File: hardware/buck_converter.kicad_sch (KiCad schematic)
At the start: 0 parts

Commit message: Adjust values of the components
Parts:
- added C1, C2, C5, C6, C7, C8, C9: 100nF, symbol Device:C
- added C3: 10µF, symbol Device:C_Polarized
- added C4: 47µF, symbol Device:C_Polarized
- added D1: 1N4007, symbol Diode:1N4007
- added D2: LED, symbol Device:LED
- added DS1: WC1602, symbol Display_Character:WC1602A
- added J1: In, symbol Connector_Generic:Conn_01x02
- added J2: Out, symbol Connector_Generic:Conn_01x02
- added J3: Nucleo, symbol Connector_Generic:Conn_02x14_Odd_Even
- added J4: MicroSD Card, symbol Connector:Micro_SD_Card
- added L1: 100µH, symbol Device:L
- added LDR1: Photo, symbol Device:R_Photo
- added Q1: IRF9540N, symbol Transistor_FET:IRF9540N
- added Q2: BC547, symbol Transistor_BJT:BC547
- added R1: 0.1Ω (5W), symbol Device:R
- added R10, R7: 100Ω, symbol Device:R
- added R11, R2, R3, R6, R8, R9: 1kΩ, symbol Device:R
- added R12: 300Ω, symbol Device:R
- added R13, R4: 10kΩ, symbol Device:R
- added R5: 8.2kΩ, symbol Device:R
- added RV1: 10kΩ, symbol Device:R_Potentiometer_Trim
- added SW1: Preset #1, symbol Switch:SW_Push
- added SW2: Preset #2, symbol Switch:SW_Push
- added SW3: Encoder, symbol Device:RotaryEncoder_Switch
- added SW4: Preset #3, symbol Switch:SW_Push
- added SW5: Preset #4, symbol Switch:SW_Push
- added U1, U2: LM358, symbol Amplifier_Operational:LM358
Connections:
- new net: D1.1 (K), L1.1, Q1.2 (D)
- new net: C4.1, C5.1, J2.1 (Pin_1), L1.2, R5.1
- new net: Q2.2 (B), R11.1
- new net: C3.1, J1.1 (Pin_1), Q1.3 (S), R4.1
- new net: Q1.1 (G), R4.2, R7.2
- new net: DS1.16 (LED(-)), R10.1
- new net: Q2.1 (C), R10.2
- new net: R8.1, U2.1, U2.2 (-)
- new net: C7.1, R8.2, R9.1
- new net: C9.1, R9.2, U2.5 (+)
- new net: C1.1, R2.2, R3.1
- new net: C6.1, R3.2, U1.5 (+)
- new net: DS1.3 (VO), RV1.2
- new net: R2.1, U1.1, U1.2 (-)
- new net: D2.2 (A), R12.2
- new net +3.3V: C2.1, C8.1, DS1.15 (LED(+)), DS1.2 (VDD), J3.2 (Pin_2), J4.4 (VDD), LDR1.1, RV1.1, U1.8 (V+), U2.8 (V+)
- new net BCKL: J3.3 (Pin_3), R11.2
- new net CURRENT: C7.2, J3.9 (Pin_9), U2.6 (-), U2.7
- new net GND: C2.2, C3.2, C4.2, C5.2, C6.2, C8.2, C9.2, D1.2 (A), D2.1 (K), DS1.1 (VSS), DS1.5 (R/W), J1.2 (Pin_2), J3.28 (Pin_28), J4.6 (VSS), J4.9 (SHIELD), Q2.3 (E), R1.1, R13.2, R6.2, RV1.3, SW1.2, SW2.2, SW3.C, SW3.S2, SW4.2, SW5.2, U1.4 (V-), U2.4 (V-)
- new net INT1: J3.19 (Pin_19), SW3.A
- new net INT2: J3.21 (Pin_21), SW3.B
- new net I_{out}: J2.2 (Pin_2), R1.2, U2.3 (+)
- new net KEY: J3.1 (Pin_1), R7.1
- new net LCD_D4: DS1.11 (D4), J3.8 (Pin_8)
- new net LCD_D5: DS1.12 (D5), J3.10 (Pin_10)
- new net LCD_D6: DS1.13 (D6), J3.12 (Pin_12)
- new net LCD_D7: DS1.14 (D7), J3.14 (Pin_14)
- new net LCD_E: DS1.6 (E), J3.4 (Pin_4)
- new net LCD_RS: DS1.4 (RS), J3.6 (Pin_6)
- new net OC_LED: J3.25 (Pin_25), R12.1
- new net PHOTO: J3.5 (Pin_5), LDR1.2, R13.1
- new net SDMMC_CLK: J3.18 (Pin_18), J4.5 (CLK)
- new net SDMMC_CMD: J3.16 (Pin_16), J4.3 (CMD)
- new net SDMMC_D0: J3.20 (Pin_20), J4.7 (DAT0)
- new net SDMMC_D1: J3.22 (Pin_22), J4.8 (DAT1)
- new net SDMMC_D2: J3.24 (Pin_24), J4.1 (DAT2)
- new net SDMMC_D3: J3.26 (Pin_26), J4.2 (DAT3/CD)
- new net SW1: J3.11 (Pin_11), SW1.1
- new net SW2: J3.13 (Pin_13), SW2.1
- new net SW3: J3.15 (Pin_15), SW4.1
- new net SW4: J3.17 (Pin_17), SW5.1
- new net SW5: J3.23 (Pin_23), SW3.S1
- new net VOLTAGE: C1.2, J3.7 (Pin_7), U1.6 (-), U1.7
- new net V_{out}: R5.2, R6.1, U1.3 (+)
- no-connect marks 0 -> 5
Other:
- note added: "Converter"
- note added: "For ERC"
- note added: "Input"
- note added: "LCD"
- note added: "Light sensor"
- note added: "Low-pass filters"
- note added: "Max. 3.261V"
- note added: "Nucleo Board"
- note added: "OC LED"
- note added: "SD Card"
- note added: "f_{c} ≈ 1.5kHz"

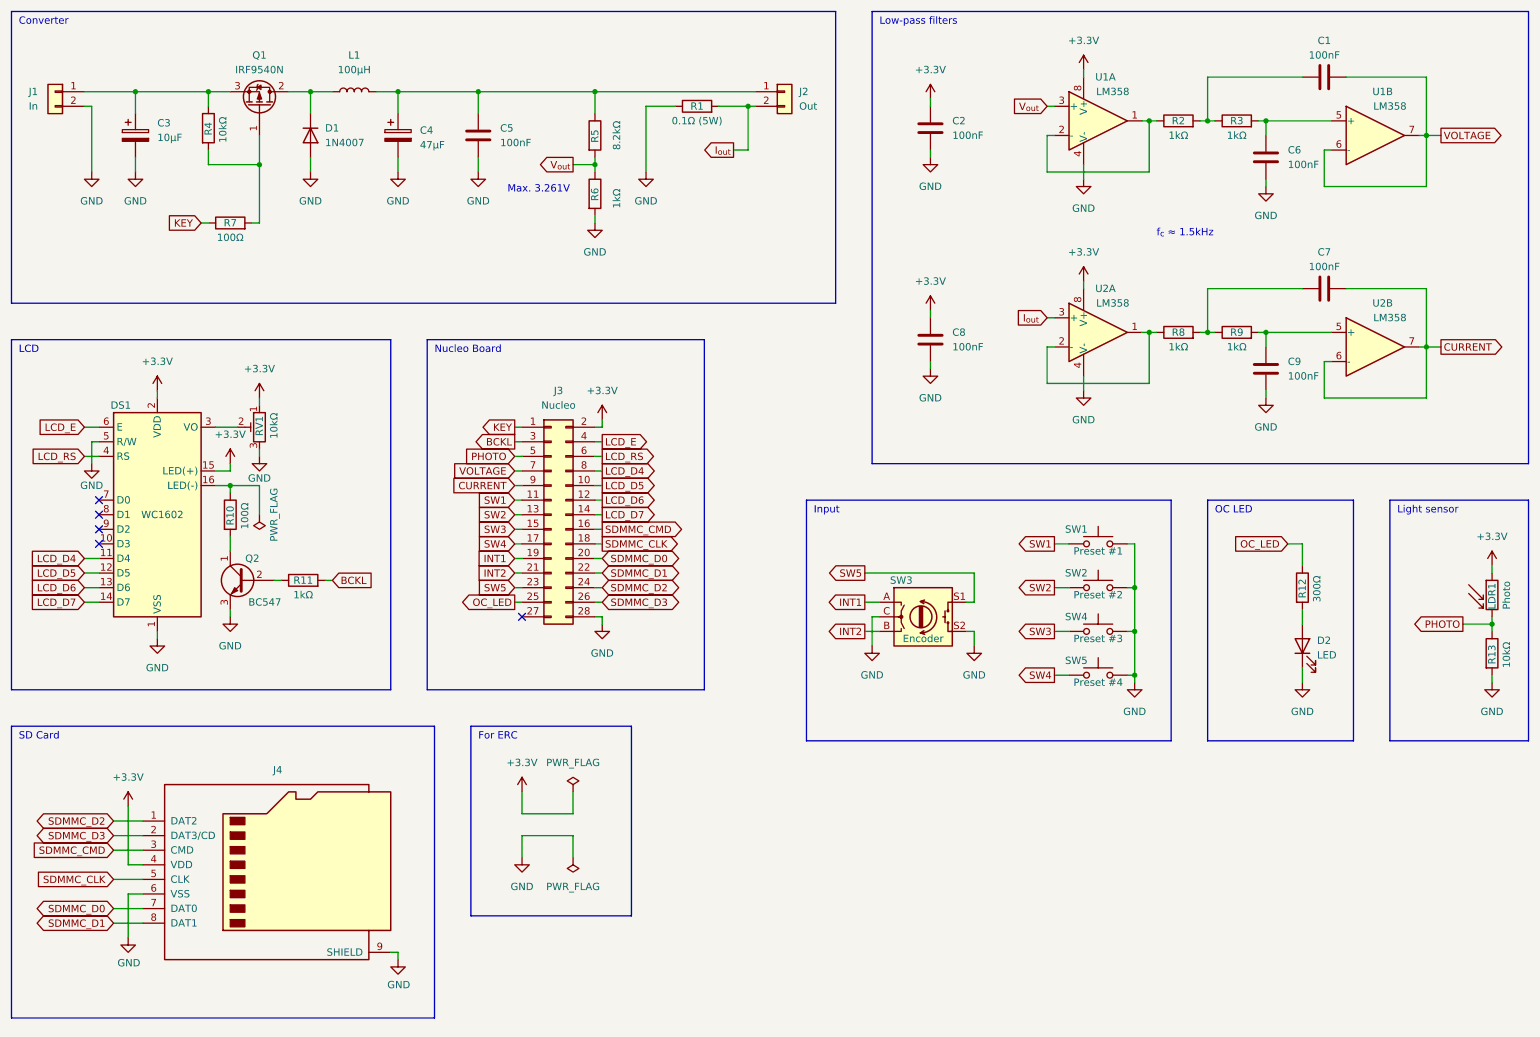
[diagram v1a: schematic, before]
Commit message: Add buttons and LEDs to the configuration
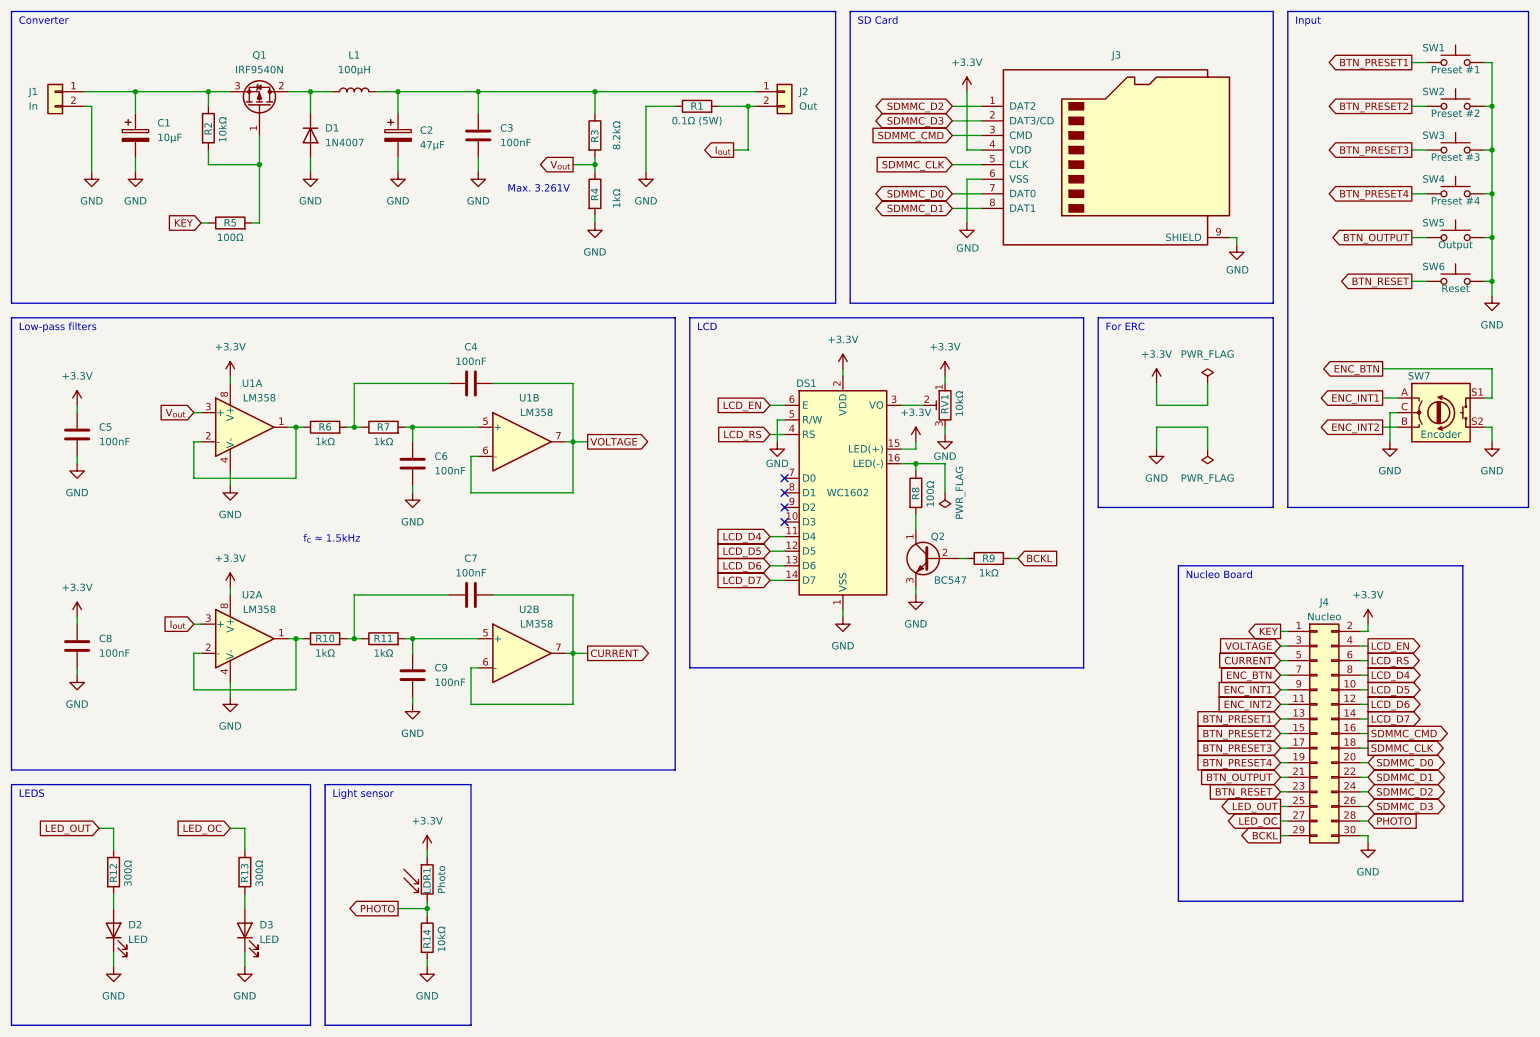
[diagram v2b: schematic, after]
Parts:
- added D3: LED, symbol Device:LED
- added R13: 300Ω, symbol Device:R
- added SW5: Output, symbol Switch:SW_Push
- added SW6: Reset, symbol Switch:SW_Push
- J4: renamed from J3; symbol Connector_Generic:Conn_02x14_Odd_Even -> Connector_Generic:Conn_02x15_Odd_Even
- renumbered C3 to C1, C4 to C2, C5 to C3, C1 to C4, C2 to C5, J4 to J3, R8 to R10, R9 to R11, R13 to R14, R4 to R2, R5 to R3, R6 to R4, R7 to R5, R2 to R6, R3 to R7, R10 to R8, R11 to R9, SW4 to SW3, SW5 to SW4, SW3 to SW7
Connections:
- net BCKL: now also J4.29 (Pin_29); no longer J4.3 (Pin_3)
- net CURRENT: now also J4.5 (Pin_5); no longer J4.9 (Pin_9)
- net GND: now also J4.30 (Pin_30), D3.1 (K), SW5.2, SW6.2; no longer J4.28 (Pin_28)
- net PHOTO: now also J4.28 (Pin_28); no longer J4.5 (Pin_5)
- net VOLTAGE: now also J4.3 (Pin_3); no longer J4.7 (Pin_7)
- net LED_OC: now reaches J4.27 (Pin_27)
- net LED_OC: now also R13.1
- net INT1 renamed BTN_PRESET4
- net BTN_PRESET4: now also SW4.1; no longer SW7.A
- net INT2 renamed BTN_OUTPUT
- net BTN_OUTPUT: now also SW5.1; no longer SW7.B
- net LCD_E renamed LCD_EN
- net OC_LED renamed LED_OUT
- net SW1 renamed BTN_PRESET1
- net BTN_PRESET1: now also J4.13 (Pin_13); no longer J4.11 (Pin_11)
- net SW2 renamed BTN_PRESET2
- net BTN_PRESET2: now also J4.15 (Pin_15); no longer J4.13 (Pin_13)
- net SW3 renamed BTN_PRESET3
- net BTN_PRESET3: now also J4.17 (Pin_17); no longer J4.15 (Pin_15)
- removed net SW4: J4.17 (Pin_17), SW4.1
- net SW5 renamed BTN_RESET
- net BTN_RESET: now also SW6.1; no longer SW7.S1
- new net: D3.2 (A), R13.2
- new net ENC_BTN: J4.7 (Pin_7), SW7.S1
- new net ENC_INT1: J4.9 (Pin_9), SW7.A
- new net ENC_INT2: J4.11 (Pin_11), SW7.B
- no-connect marks 5 -> 4
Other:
- note added: "LEDS"
- note removed: "OC LED"
- moved on the sheet: C4, C5, C6, C7, C8, C9, D2, DS1, J3, LDR1, Q2, R10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

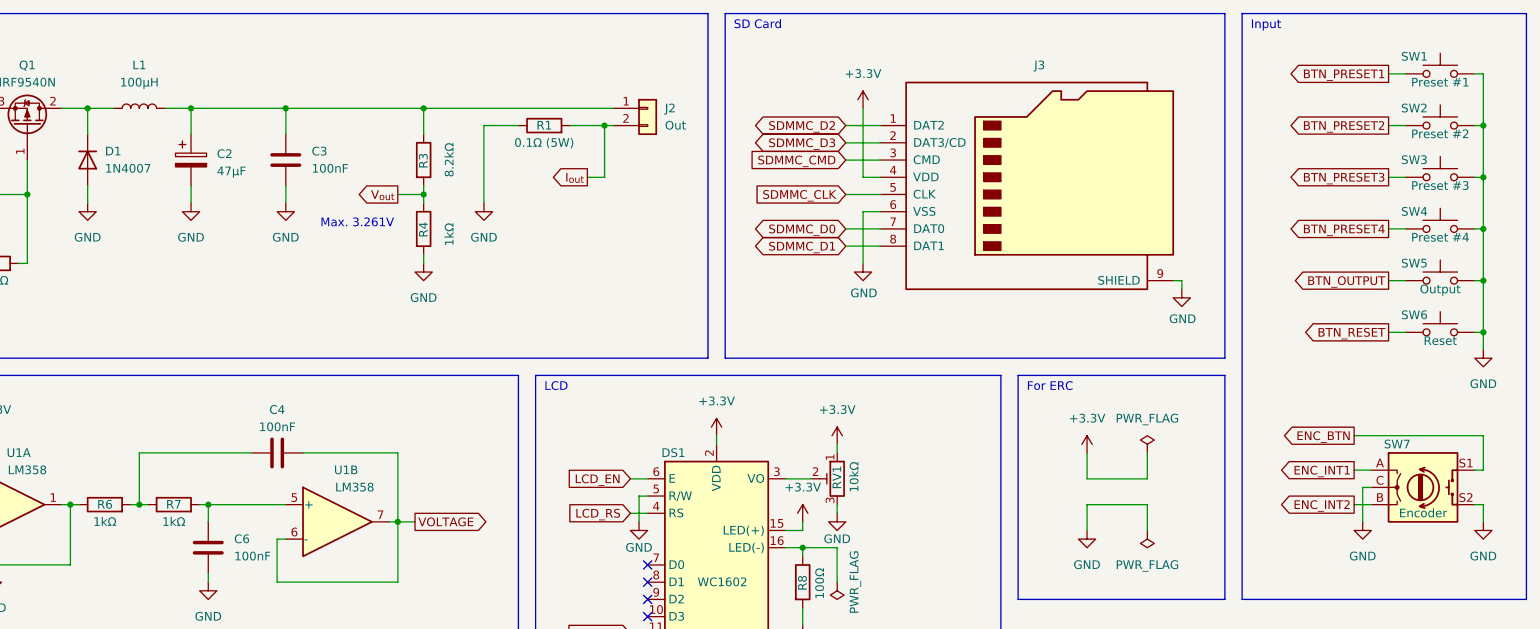
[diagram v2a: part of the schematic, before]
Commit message: Update KiCad project version
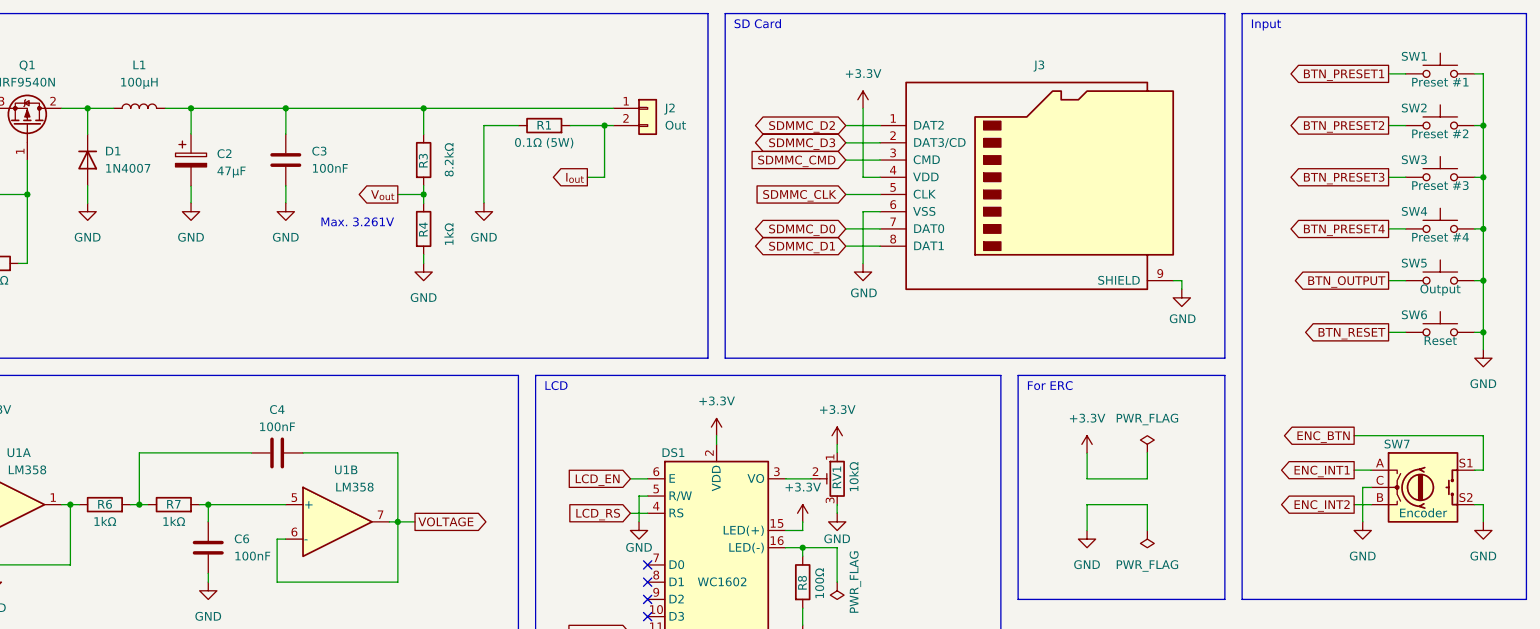
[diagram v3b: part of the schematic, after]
